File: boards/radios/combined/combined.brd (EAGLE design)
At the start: 22.7 x 30 mm, 16 parts

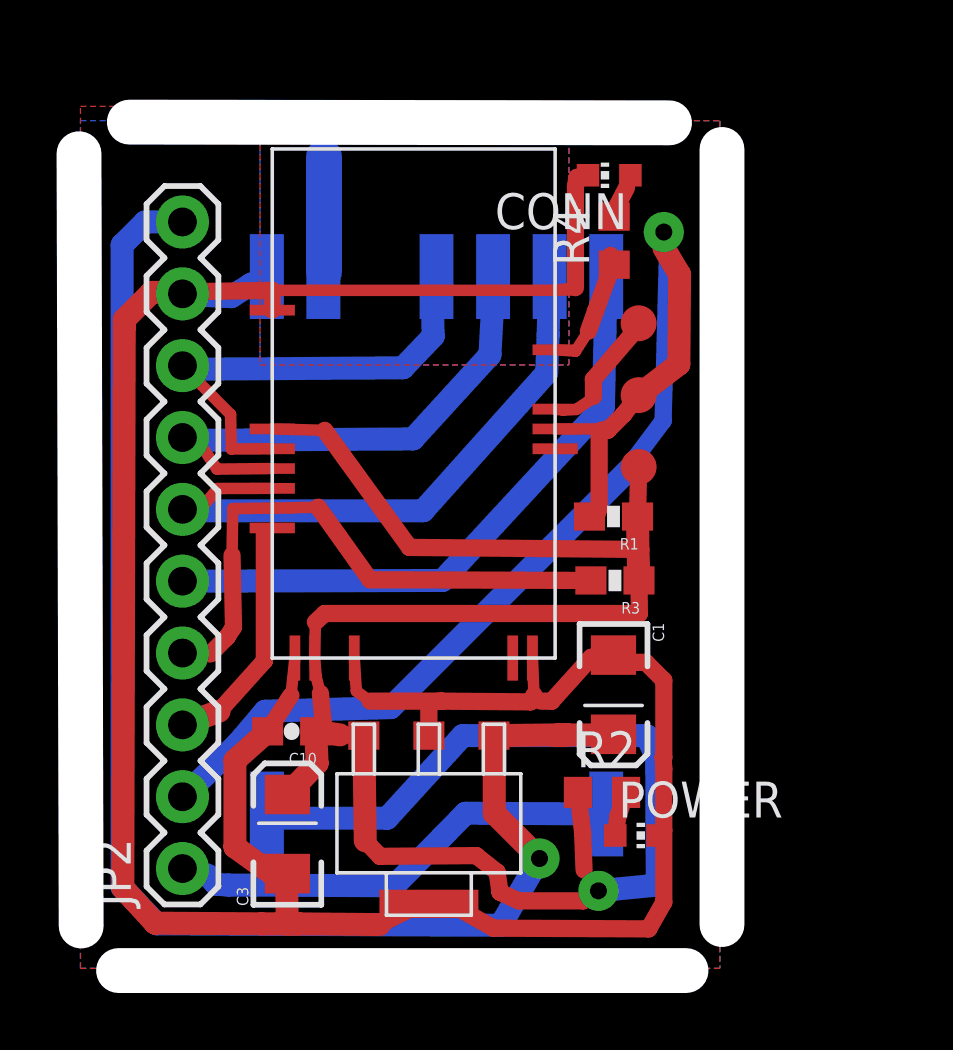
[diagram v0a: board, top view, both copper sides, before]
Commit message: updated radio with better regulator
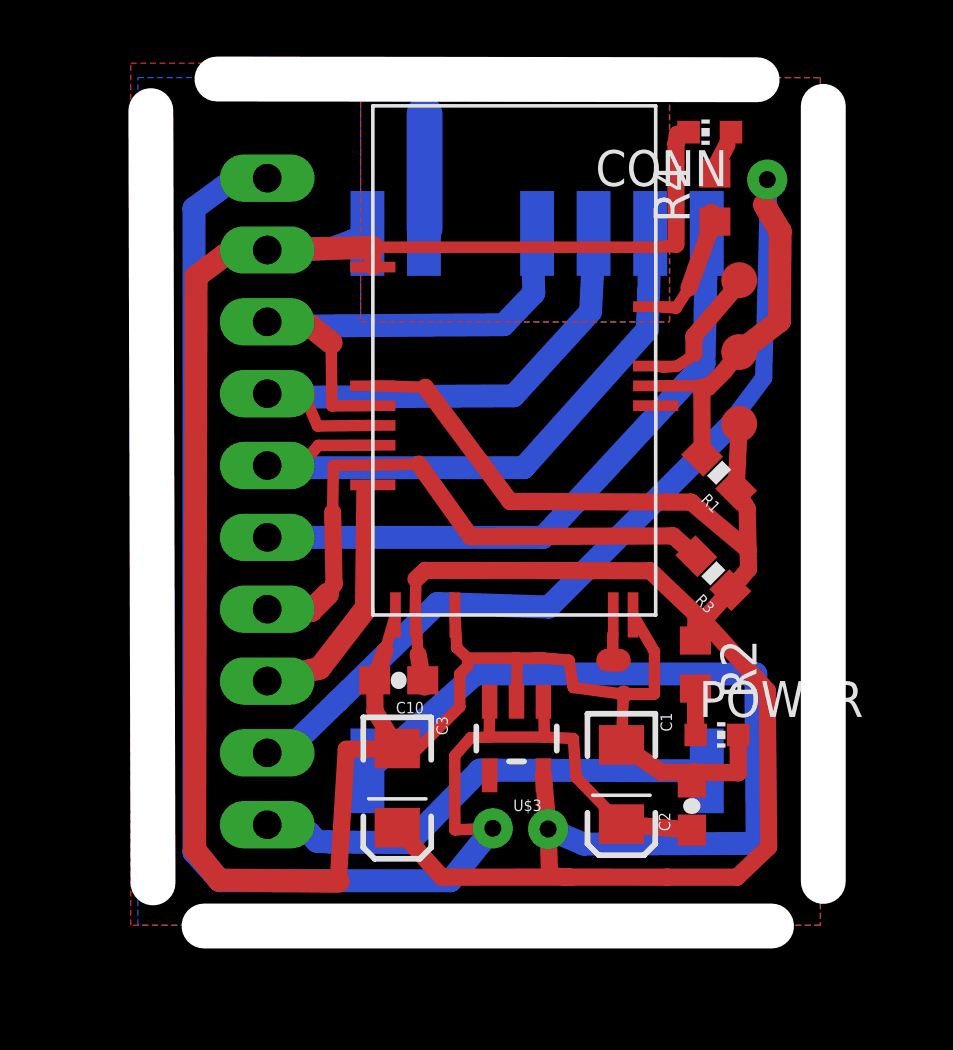
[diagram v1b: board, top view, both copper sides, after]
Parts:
- removed JP2: M10", SparkFun-Connectors:1X10
- added C2: 1uF, SparkFun:0603-CAP
- added U$2: HEADER-10, homemade-hardware:HEADER-10
- U$3: value REGULATOR3.3V-UA78M33CDCYR -> REGULATOR3.3V-MIC5205; device ITP_Lab:SOT223 -> homemade-hardware:SOT23-5
- moved R2 5.60 mm to (20.5, 10.2), turned to 270 degrees
- moved POWER 4.55 mm to (21.2, 7.75)
- moved U$3 4.31 mm to (14.1, 7.62)
- moved C3 4.21 mm to (9.93, 5.87), turned to 270 degrees
- moved C10 4.19 mm to (9.98, 9.68)
- moved R1 4.04 mm to (21.3, 17.0), turned to 135 degrees
- moved CONN 3.87 mm to (21.0, 29.1)
- moved R4 3.87 mm to (21.2, 26.7)
- moved U$5 3.87 mm to (14.1, 19.6)
- moved U$1 3.87 mm to (15.9, 16.0)
- moved CLOCK1 3.87 mm to (22.0, 21.3)
- moved VCC 3.87 mm to (22.0, 18.7)
- moved CLOCK 3.87 mm to (22.0, 23.8)
- moved R3 3.49 mm to (21.1, 13.5), turned to 135 degrees
- moved C1 3.19 mm to (17.9, 5.99)
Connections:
- net BT-REQ: now also U$2.3; no longer JP2.3
- net BT-SS: now also U$2.4; no longer JP2.4
- net GND: now also C2.2, U$2.9; no longer JP2.9, U$3.4
- net MISO: now also U$2.7; no longer JP2.7
- net MOSI: now also U$2.6; no longer JP2.6
- net RF-REQ: now also U$2.1; no longer JP2.1
- net RF-SS: now also U$2.5; no longer JP2.5
- net SCK: now also U$2.8; no longer JP2.8
- net SWDIO/RST: now also U$2.2; no longer JP2.2
- net VCC: now also U$3.5; no longer U$3.3
- net VIN: now also C2.1, U$2.10, U$3.3; no longer JP2.10
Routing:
- net VCC: track 79.4 -> 95.8 mm
- net GND: track 101.9 -> 91.9 mm
- net SCK: track 16.6 -> 18.2 mm
- net MISO: track 18.8 -> 20.1 mm
- net MOSI: track 22.0 -> 23.1 mm
- net BT-SS: track 20.4 -> 21.4 mm
- net N$7: track 0.00 -> 0.94 mm
- net RF-SS: track 22.2 -> 22.7 mm
- net RF-REQ: track 16.3 -> 16.8 mm
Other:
- board size 22.7 x 30 mm -> 23.8 x 29.9 mm
